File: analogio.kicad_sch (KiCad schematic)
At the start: 92 parts, among them J10 1VOCT1_IN, J11 1VOCT2_IN, J12 MAIN_OUT1, J13 MAIN_OUT2, J14 MAIN_OUT4, J15 MAIN_OUT3, J5 CV1_INPUT, J6 CV2_INPUT, J7 CV3_INPUT, J8 CV4_INPUT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

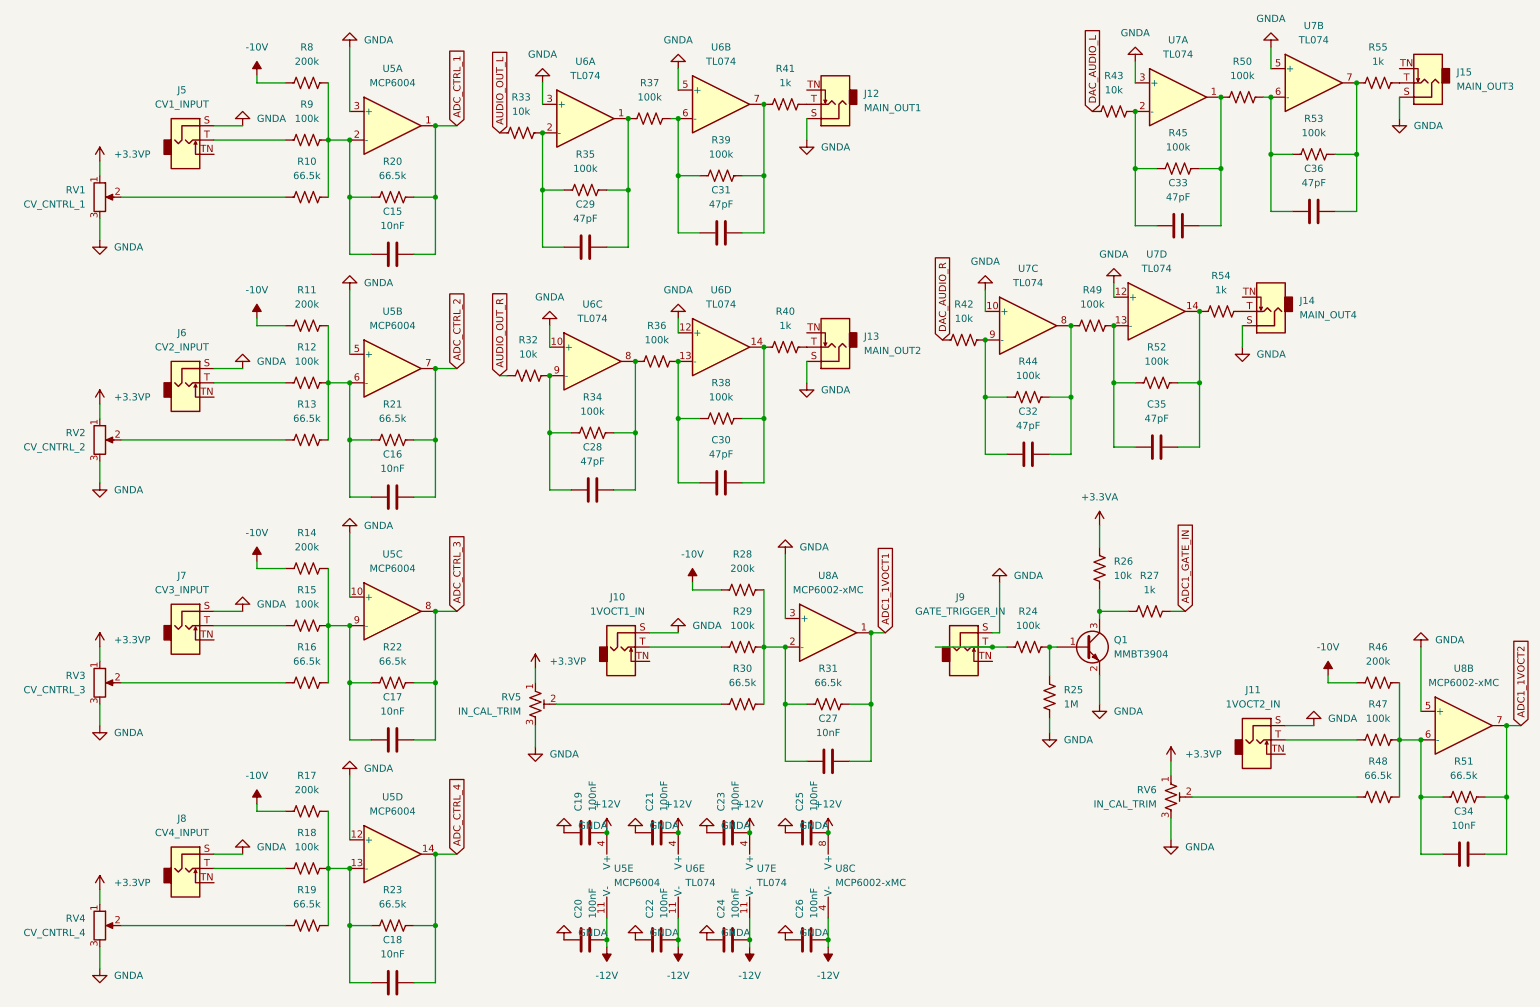
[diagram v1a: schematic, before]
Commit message: Version update
Added DC/DC power block and opAmps for audio input. Redesigned PCB completely moving all components to one side so that it can lay flat.
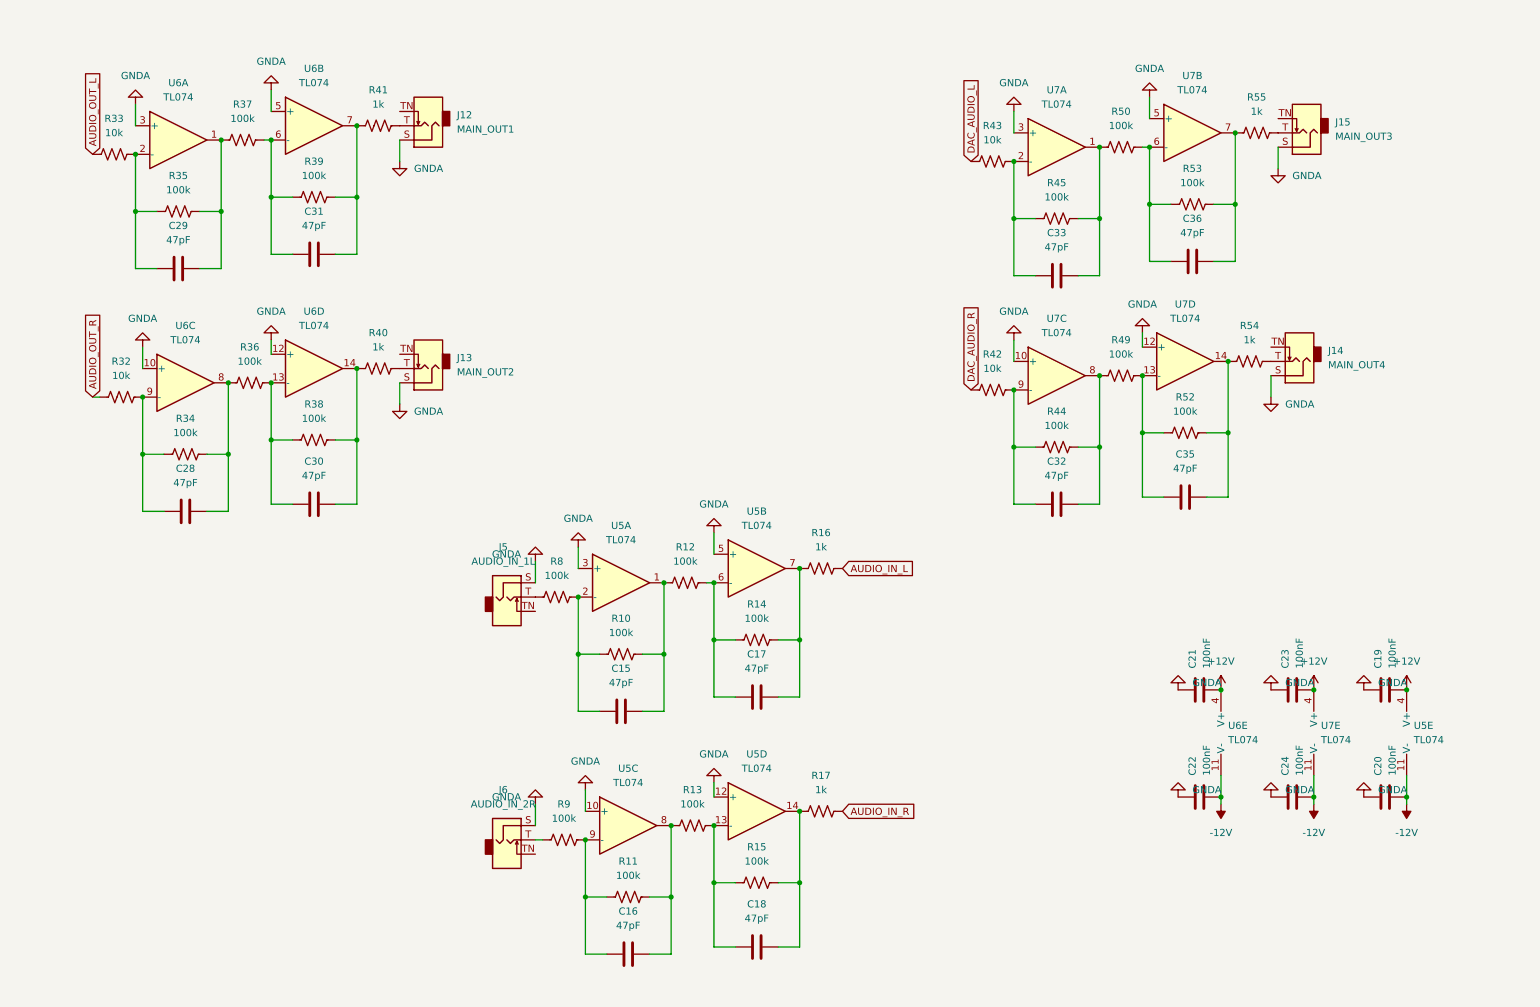
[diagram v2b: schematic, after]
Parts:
- removed C25, C26: 100nF, Capacitor_SMD:C_0805_2012Metric, symbol Device:C
- removed C27, C34: 10nF, Capacitor_SMD:C_0805_2012Metric, symbol Device:C
- removed J10: 1VOCT1_IN, Connector_Audio:Jack_3.5mm_QingPu_WQP-PJ398SM_Vertical_CircularHoles, symbol Connector:AudioJack2_SwitchT
- removed J11: 1VOCT2_IN, Connector_Audio:Jack_3.5mm_QingPu_WQP-PJ398SM_Vertical_CircularHoles, symbol Connector:AudioJack2_SwitchT
- removed J7: CV3_INPUT, Connector_Audio:Jack_3.5mm_QingPu_WQP-PJ398SM_Vertical_CircularHoles, symbol Connector:AudioJack2_SwitchT
- removed J8: CV4_INPUT, Connector_Audio:Jack_3.5mm_QingPu_WQP-PJ398SM_Vertical_CircularHoles, symbol Connector:AudioJack2_SwitchT
- removed J9: GATE_TRIGGER_IN, Connector_Audio:Jack_3.5mm_QingPu_WQP-PJ398SM_Vertical_CircularHoles, symbol Connector:AudioJack2_SwitchT
- removed Q1: MMBT3904, Package_TO_SOT_SMD:SOT-23, symbol Transistor_BJT:MMBT3904
- removed R18, R24, R29, R47: 100k, Resistor_SMD:R_0805_2012Metric, symbol Device:R_US
- removed R19, R20, R21, R22, R23, R30, R31, R48, R51: 66.5k, Resistor_SMD:R_0805_2012Metric, symbol Device:R_US
- removed R25: 1M, Resistor_SMD:R_0805_2012Metric, symbol Device:R_US
- removed R26: 10k, Resistor_SMD:R_0805_2012Metric, symbol Device:R_US
- removed R27: 1k, Resistor_SMD:R_0805_2012Metric, symbol Device:R_US
- removed R28, R46: 200k, Resistor_SMD:R_0805_2012Metric, symbol Device:R_US
- removed RV1: CV_CNTRL_1, Potentiometer_THT:Potentiometer_Alpha_RD901F-40-00D_Single_Vertical, symbol Device:R_Potentiometer
- removed RV2: CV_CNTRL_2, Potentiometer_THT:Potentiometer_Alpha_RD901F-40-00D_Single_Vertical, symbol Device:R_Potentiometer
- removed RV3: CV_CNTRL_3, Potentiometer_THT:Potentiometer_Alpha_RD901F-40-00D_Single_Vertical, symbol Device:R_Potentiometer
- removed RV4: CV_CNTRL_4, Potentiometer_THT:Potentiometer_Alpha_RD901F-40-00D_Single_Vertical, symbol Device:R_Potentiometer
- removed RV5, RV6: IN_CAL_TRIM, Potentiometer_THT:Potentiometer_Bourns_3266W_Vertical, symbol Device:R_Potentiometer_Trim_US
- removed U5: MCP6004, Package_SO:TSSOP-14_4.4x5mm_P0.65mm, symbol Amplifier_Operational:MCP6004
- removed U8: MCP6002-xMC, Package_DFN_QFN:DFN-8-1EP_3x2mm_P0.5mm_EP1.75x1.45mm, symbol Amplifier_Operational:MCP6002-xMC
- added U5: TL074, Package_SO:SOIC-14_3.9x8.7mm_P1.27mm, symbol Amplifier_Operational:TL074
- C15, C16, C17, C18: value 10nF -> 47pF
- J5: value CV1_INPUT -> AUDIO_IN_1L
- J6: value CV2_INPUT -> AUDIO_IN_2R
- R10, R13: value 66.5k -> 100k
- R11, R14, R8: value 200k -> 100k
- R16: value 66.5k -> 1k
- R17: value 200k -> 1k
- U6, U7: footprint Package_DIP:SMDIP-14_W9.53mm -> Package_SO:SOIC-14_3.9x8.7mm_P1.27mm
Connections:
- net ADC_CTRL_2 is gone; now on an unnamed net: C16.2
- net ADC_CTRL_3 is gone; now on an unnamed net: C17.2
- net +12V: now also U5.4 (V+)
- net -12V: now also U5.11 (V-)
- net GNDA: now also U5.10 (+), U5.12 (+), U5.3 (+), U5.5 (+)
- net at R10.2: now also C15.1, R8.1, U5.2 (-)
- net at R13.2: now also R11.1, U5.8
- net at J6.T: now also R9.2; no longer R12.2
- net at R16.2: now also R14.1, U5.7
- net at C18.1: now also R13.1, R15.2, U5.13 (-); no longer R17.1
- net at J5.T: now also R8.2; no longer R9.2
- removed net -10V: R11.2, R14.2, R17.2, R8.2
- net ADC_CTRL_1: no longer names the net of C15.2
- net ADC_CTRL_1: now also R10.1, R12.2, U5.1
- net ADC_CTRL_4: no longer names the net of C18.2
- net ADC_CTRL_4: now also R15.1, R17.2, U5.14
- new net: C16.1, R11.2, R9.1, U5.9 (-)
- new net: C17.1, R12.1, R14.2, U5.6 (-)
- new net AUDIO_IN_L: R16.1
- new net AUDIO_IN_R: R17.1
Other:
- moved on the sheet: C21, C22, C23, C24, C28, C29, C30, C31, C32, C33, C35, C36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
